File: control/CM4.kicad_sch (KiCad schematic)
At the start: 2 parts, among them SW2 SW_Push

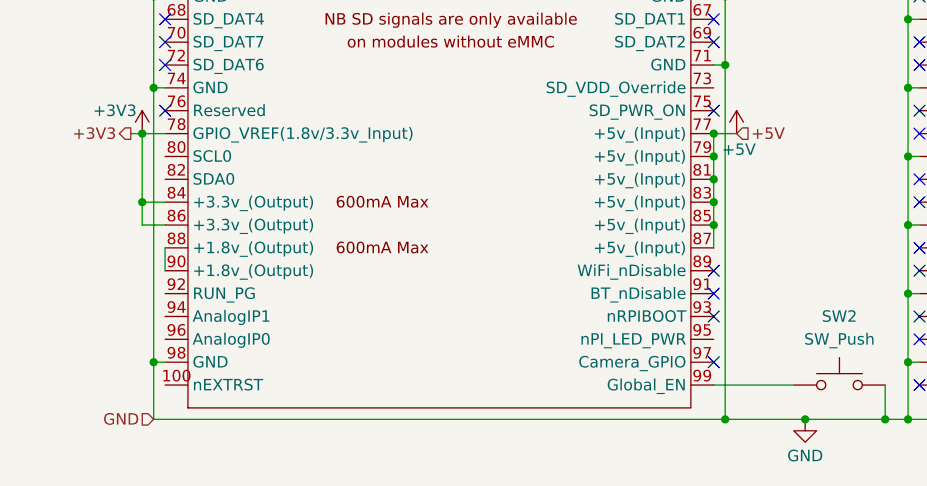
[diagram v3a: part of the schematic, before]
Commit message: Daughterboard setup, labeling, and testpoints
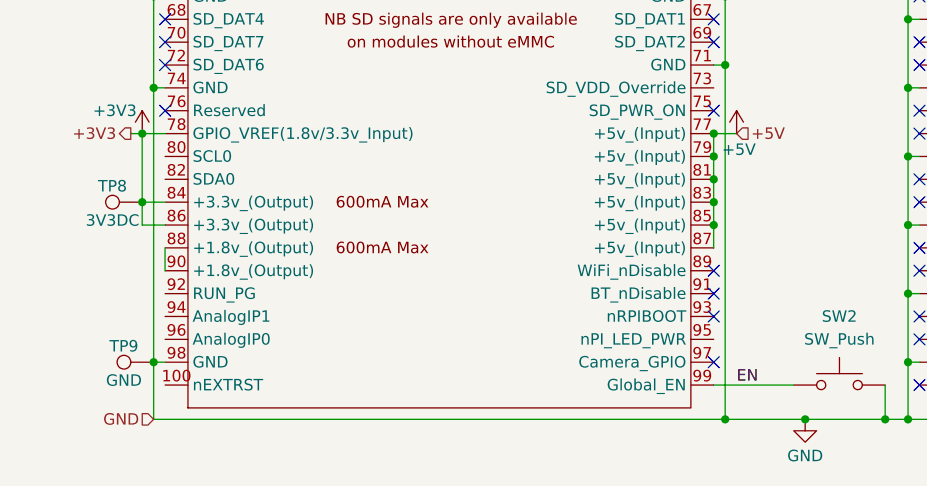
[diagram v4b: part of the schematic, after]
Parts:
- added TP8: 3V3DC, symbol Connector:TestPoint
- added TP9: GND, symbol Connector:TestPoint
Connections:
- net +3V3: now also TP8.1
- net GND: now also TP9.1
- net EN: now reaches Module1.99 (Global_EN), SW2.1
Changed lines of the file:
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@@
+		)
+	)
+	(label "EN"
+		(at 106.68 153.67 0)
+		(fields_autoplaced yes)
+		(effects
+			(font
+				(size 1.27 1.27)
+			)
+			(justify left bottom)
 		)
 	)
@@
 	)
 	(symbol
+		(lib_id "Connector:TestPoint")
+		(at 40.64 133.35 90)
+		(unit 1)
+		(exclude_from_sim no)
+		(in_bom yes)
+		(on_board yes)
+		(dnp no)
+		(property "Reference" "TP8"
+			(at 37.338 131.572 90)
+			(effects
+				(font
+					(size 1.27 1.27)
+				)
+			)
+		)
+		(property "Value" "3V3DC"
+			(at 37.338 135.382 90)
+			(effects
+				(font
+					(size 1.27 1.27)
+				)
+			)
+		)
+		(property "Footprint" ""
+			(at 40.64 128.27 0)
+			(effects
+				(font
+					(size 1.27 1.27)
+				)
+				(hide yes)
+			)
+		)
+		(property "Datasheet" "~"
+			(at 40.64 128.27 0)
+			(effects
+				(font
+					(size 1.27 1.27)
+				)
+				(hide yes)
+			)
+		)
+		(property "Description" "test point"
+			(at 40.64 133.35 0)
+			(effects
+				(font
+					(size 1.27 1.27)
+				)
+				(hide yes)
+			)
+		)
+		(pin "1"
+		)
+		(instances
+			(project ""
+				(path "/f45f1ed7-9099-407f-b6ad-6cac15e7865f/5e58b04a-ae38-42c8-ade5-91d029711ef9"
+					(reference "TP8")
+					(unit 1)
+				)
+			)
+		)
+	)
+	(symbol
 		(lib_id "Switch:SW_Push")
 		(at 118.11 153.67 0)
@@
 				)
 			)
+		)
+	)
+	(symbol
+		(lib_id "Connector:TestPoint")
+		(at 41.91 151.13 90)
+		(unit 1)
+		(exclude_from_sim no)
+		(in_bom yes)
+		(on_board yes)
+		(dnp no)
+		(property "Reference" "TP9"
+			(at 38.608 149.352 90)
+			(effects
+				(font
+					(size 1.27 1.27)
+				)
+			)
+		)
+		(property "Value" "GND"
+			(at 38.608 153.162 90)
+			(effects
+				(font
+					(size 1.27 1.27)
+				)
+			)
+		)
+		(property "Footprint" ""
+			(at 41.91 146.05 0)
+			(effects
+				(font
+					(size 1.27 1.27)
+				)
+				(hide yes)
+			)
+		)
+		(property "Datasheet" "~"
+			(at 41.91 146.05 0)
+			(effects
+				(font
+					(size 1.27 1.27)
+				)
+				(hide yes)
+			)
+		)
+		(property "Description" "test point"
+			(at 41.91 151.13 0)
+			(effects
+				(font
+					(size 1.27 1.27)
+				)
+				(hide yes)
+			)
+		)
+		(pin "1"
+		)
+		(instances
+			(project "control"
+				(path "/f45f1ed7-9099-407f-b6ad-6cac15e7865f/5e58b04a-ae38-42c8-ade5-91d029711ef9"
+					(reference "TP9")
+					(unit 1)
+				)
+			)
